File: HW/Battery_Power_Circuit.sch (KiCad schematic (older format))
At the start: 10 parts

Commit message: What did I do?
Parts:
- removed BT? (x2): Battery, symbol Battery
- added BT? (x2): 18650, symbol Battery_Cell
- added D?: 1N4448W, symbol D_ALT
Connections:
- wire segments 29 -> 33
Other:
- note added: "+"
- note added: "-"
- note added: "3.7V"
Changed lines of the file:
@@
 $EndDescr
-$Comp
-L Battery BT?
-U 1 1 5B317E9C
-P 6800 2400
-F 0 "BT?" H 6900 2500 50  0000 L CNN
-F 1 "Battery" H 6900 2400 50  0000 L CNN
-F 2 "" V 6800 2460 50  0001 C CNN
-F 3 "" V 6800 2460 50  0001 C CNN
-	1    6800 2400
-	1    0    0    -1
-$EndComp
-$Comp
-L Battery BT?
-U 1 1 5B32E42C
-P 6500 3750
-F 0 "BT?" H 6150 3850 50  0000 L CNN
-F 1 "Battery" H 6150 3750 50  0000 L CNN
-F 2 "" V 6500 3810 50  0001 C CNN
-F 3 "" V 6500 3810 50  0001 C CNN
-	1    6500 3750
-	1    0    0    -1
-$EndComp
 $Comp
 L VBUS #PWR?
@@
 NoConn ~ 6300 3350
 Wire Wire Line
-	6500 3350 6500 3550
+	6500 3350 6500 3600
 Wire Wire Line
 	6800 2750 6800 2600
 Wire Wire Line
-	6800 1850 6800 2200
+	6800 1850 6800 2300
 Wire Wire Line
 	6050 2000 6800 2000
@@
 	6900 4050 6500 4050
 Wire Wire Line
-	6500 3950 6500 4150
+	6500 3900 6500 4150
 $Comp
 L GND #PWR?
@@
 Wire Notes Line
 	3300 4650 5950 4650
+$Comp
+L Battery_Cell BT?
+U 1 1 5B34706B
+P 6500 3800
+F 0 "BT?" H 6600 3950 50  0000 L CNN
+F 1 "18650" H 6500 3750 50  0000 L CNN
+F 2 "" V 6500 3860 50  0001 C CNN
+F 3 "" V 6500 3860 50  0001 C CNN
+	1    6500 3800
+	1    0    0    -1
+$EndComp
+$Comp
+L Battery_Cell BT?
+U 1 1 5B3470A3
+P 6800 2500
+F 0 "BT?" H 6900 2600 50  0000 L CNN
+F 1 "18650" H 6900 2500 50  0000 L CNN
+F 2 "" V 6800 2560 50  0001 C CNN
+F 3 "" V 6800 2560 50  0001 C CNN
+	1    6800 2500
+	1    0    0    -1
+$EndComp
+Text Notes 6500 2500 0    60   ~ 0
+3.7V
+Text Notes 6150 3800 0    60   ~ 0
+3.7V
+Text Notes 6300 3700 0    60   ~ 0
++
+Text Notes 6300 3900 0    60   ~ 0
+-
+Text Notes 6650 2400 0    60   ~ 0
++
+Text Notes 6650 2600 0    60   ~ 0
+-
+$Comp
+L D_ALT D?
+U 1 1 5B34A2E5
+P 7700 3050
+F 0 "D?" H 7700 3150 50  0000 C CNN
+F 1 "1N4448W" H 7700 2950 50  0000 C CNN
+F 2 "" H 7700 3050 50  0001 C CNN
+F 3 "" H 7700 3050 50  0001 C CNN
+	1    7700 3050
+	0    1    1    0
+$EndComp
+Wire Wire Line
+	7700 2900 7700 2600
+Wire Wire Line
+	7700 2600 7200 2600
+Connection ~ 7200 2600
+Wire Wire Line
+	7700 3200 7700 3450
+Wire Wire Line
+	7700 3450 7200 3450
+Connection ~ 7200 3450
 $EndSCHEMATC

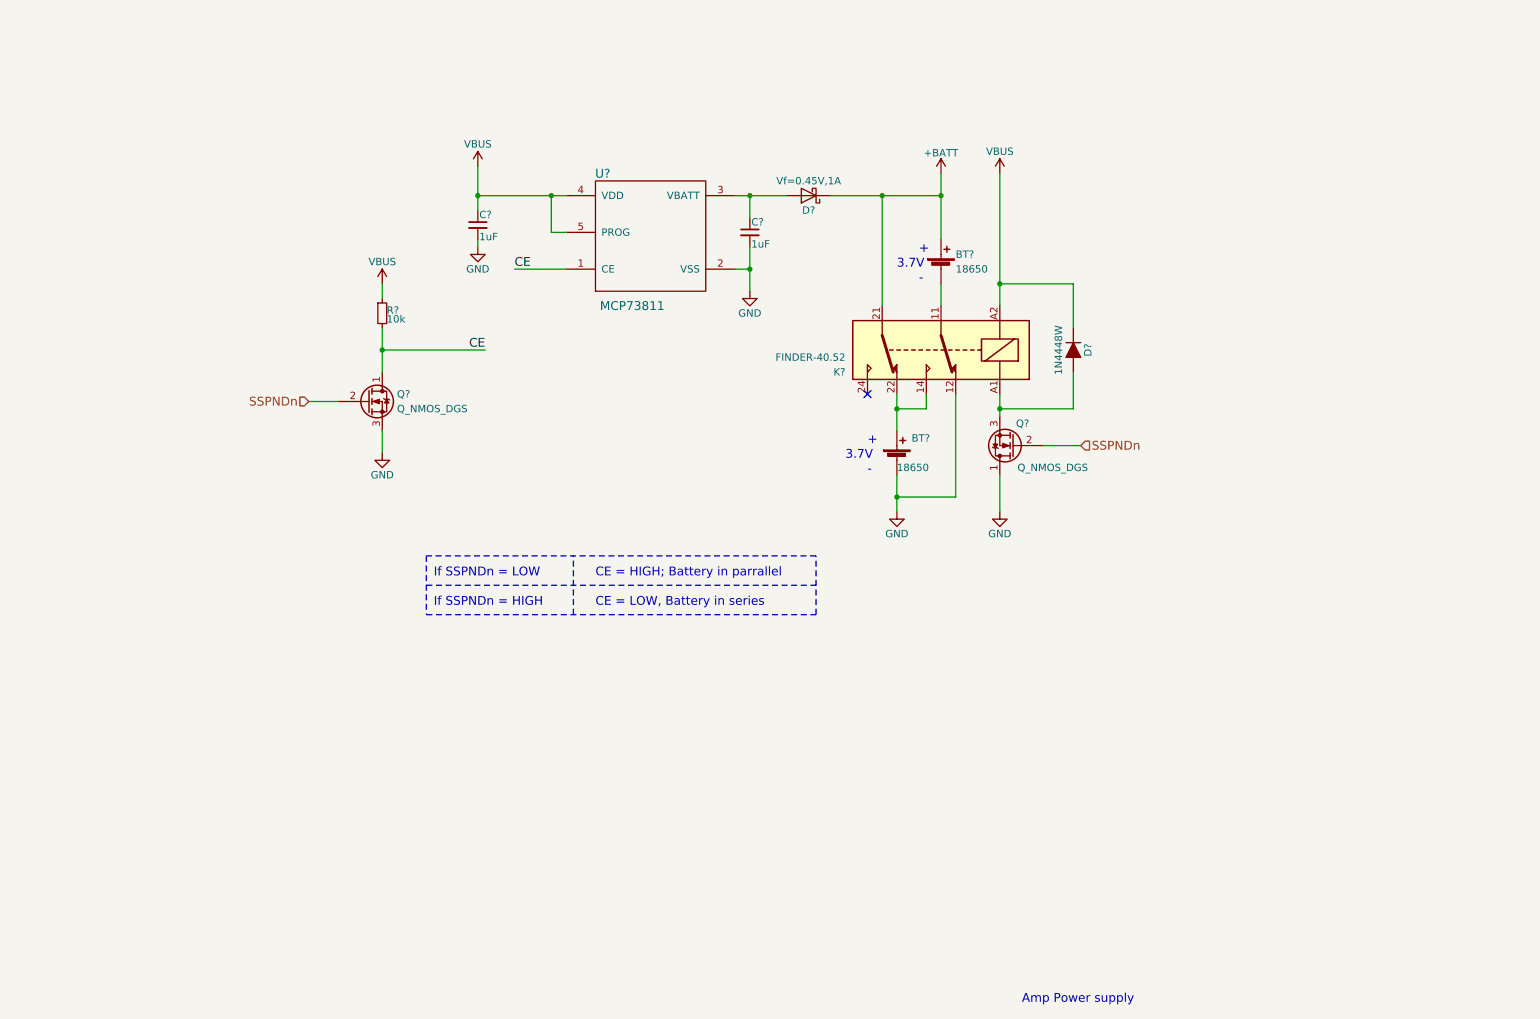
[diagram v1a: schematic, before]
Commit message: Added LEDs, Test points, and ESD protection on USB
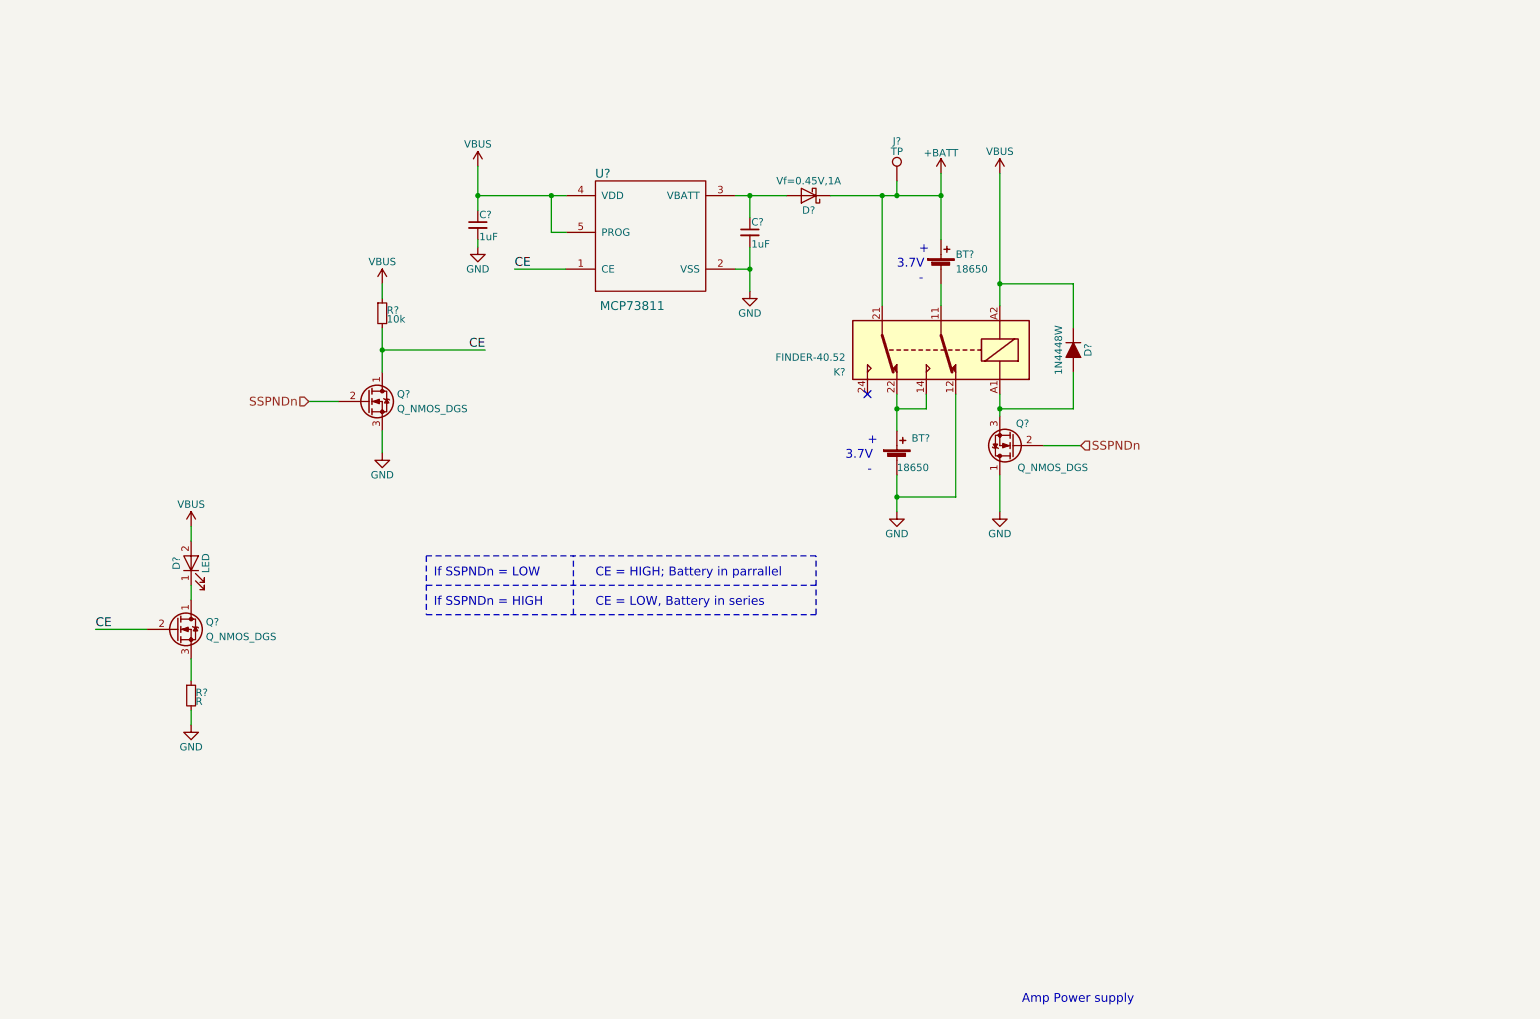
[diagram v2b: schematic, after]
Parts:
- added D?: LED, symbol LED
- added J?: TP, symbol TEST_1P
- added Q?: Q_NMOS_DGS, symbol Q_NMOS_DGS
- added R?: R, symbol R_Small
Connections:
- net +BATT: now also J?.1
- net CE: now also Q?.2 (G)
- net GND: now also R?.2
- net VBUS: now also D?.2 (A)
- new net: D?.1 (K), Q?.1 (D)
- new net: Q?.3 (S), R?.1
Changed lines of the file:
@@
 $EndComp
 Wire Wire Line
-	7200 2750 7200 1850
+	7200 1850 7200 2750
 $Comp
 L Q_NMOS_DGS Q?
@@
 $EndComp
 Wire Wire Line
-	7200 3500 7200 3350
+	7200 3350 7200 3500
 $Comp
 L GND #PWR?
@@
 	7700 3450 7200 3450
 Connection ~ 7200 3450
+$Comp
+L VBUS #PWR?
+U 1 1 5B3D1057
+P 1700 4250
+F 0 "#PWR?" H 1700 4100 50  0001 C CNN
+F 1 "VBUS" H 1700 4400 50  0000 C CNN
+F 2 "" H 1700 4250 50  0001 C CNN
+F 3 "" H 1700 4250 50  0001 C CNN
+	1    1700 4250
+	1    0    0    -1
+$EndComp
+$Comp
+L Q_NMOS_DGS Q?
+U 1 1 5B3D117C
+P 1600 4950
+F 0 "Q?" H 1800 5000 50  0000 L CNN
+F 1 "Q_NMOS_DGS" H 1800 4900 50  0000 L CNN
+F 2 "" H 1800 5050 50  0001 C CNN
+F 3 "" H 1600 4950 50  0001 C CNN
+	1    1600 4950
+	1    0    0    -1
+$EndComp
+$Comp
+L LED D?
+U 1 1 5B3D11DA
+P 1700 4500
+F 0 "D?" H 1700 4600 50  0000 C CNN
+F 1 "LED" H 1700 4400 50  0000 C CNN
+F 2 "" H 1700 4500 50  0001 C CNN
+F 3 "" H 1700 4500 50  0001 C CNN
+	1    1700 4500
+	0    -1   -1   0
+$EndComp
+Wire Wire Line
+	1700 4750 1700 4650
+Wire Wire Line
+	1700 4350 1700 4250
+Wire Wire Line
+	1400 4950 1050 4950
+Text Label 1050 4950 0    60   ~ 0
+CE
+$Comp
+L R_Small R?
+U 1 1 5B3D1363
+P 1700 5400
+F 0 "R?" H 1730 5420 50  0000 L CNN
+F 1 "R" H 1730 5360 50  0000 L CNN
+F 2 "" H 1700 5400 50  0001 C CNN
+F 3 "" H 1700 5400 50  0001 C CNN
+	1    1700 5400
+	1    0    0    -1
+$EndComp
+Wire Wire Line
+	1700 5300 1700 5150
+$Comp
+L GND #PWR?
+U 1 1 5B3D141A
+P 1700 5600
+F 0 "#PWR?" H 1700 5350 50  0001 C CNN
+F 1 "GND" H 1700 5450 50  0000 C CNN
+F 2 "" H 1700 5600 50  0001 C CNN
+F 3 "" H 1700 5600 50  0001 C CNN
+	1    1700 5600
+	1    0    0    -1
+$EndComp
+Wire Wire Line
+	1700 5600 1700 5500
+$Comp
+L TEST_1P J?
+U 1 1 5B3D6BCB
+P 6500 1900
+F 0 "J?" H 6500 2170 50  0000 C CNN
+F 1 "TP" H 6500 2100 50  0000 C CNN
+F 2 "" H 6700 1900 50  0001 C CNN
+F 3 "" H 6700 1900 50  0001 C CNN
+	1    6500 1900
+	1    0    0    -1
+$EndComp
+Wire Wire Line
+	6500 1900 6500 2000
+Connection ~ 6500 2000
 $EndSCHEMATC

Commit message: First draft done :100:
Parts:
- added C?: 1uF, symbol C_Small
- added C?: 10uF, symbol CP1_Small
- added D?: 1N4448W, symbol D_ALT
- added Q?: Q_NMOS_DGS, symbol Q_NMOS_DGS
- added U?: BA07CC0FP-E2, TO_SOT_Packages_THT:TO-252-2, symbol LF25_TO252
- D7: renamed from D?; value LED -> LED, 2.1V, 20mA
- R25: renamed from R?; value R -> 100
- gave numbers to parts that had none: 13
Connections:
- wire segments 39 -> 53
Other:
- note added: "Battery Charger"
- note added: "Battery Regulator"
- note added: "CE = LOW; Battery in series"
- note removed: "CE = LOW, Battery in series"
- moved on the sheet: J14

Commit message: First draft done :100:
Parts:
- gave numbers to parts that had none: 5

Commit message: 7V Regulator now a 5V buck converter
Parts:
- removed C75: 1uF, symbol C_Small
- removed C76: 10uF, symbol CP1_Small
- removed D15: 1N4448W, symbol D_ALT
- removed J7: TP, symbol TEST_1P
- removed Q9: Q_NMOS_DGS, symbol Q_NMOS_DGS
- removed U10: BA07CC0FP-E2, TO_SOT_Packages_THT:TO-252-2, symbol LF25_TO252
- added C?: 100uF, symbol CP1_Small
- added C?: 330uF, symbol CP1_Small
- added C?: NP, symbol CP1_Small
- added D?: 1N5819, symbol D_Schottky
- added L?: 330uH, symbol L
- added L?: 20uH, symbol L
- added R?: 0.0, symbol R
- added U?: TL2575, symbol TL2575
- D5: value Vf=0.45V,1A -> 1N5819
- K1: value FINDER-40.52 -> V23105A5001A201
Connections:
- net labels added: +5V
- wire segments 53 -> 61
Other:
- note added: "Buck Converter \n5V fixed output\n"
- note removed: "Battery Regulator"
- moved on the sheet: BT1, BT2, C35, C36, D5, D6, D7, K1, Q2, Q3, Q4, R24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

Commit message: Buck and fp
Changed buck to one with 3A output. Started fp association
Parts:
- removed U?: TL2575, symbol TL2575
- added U5: LM2576, TO_SOT_Packages_SMD:TO-263-5_TabPin6, symbol LM2576
- L8: renamed from L?; value 20uH -> NP
- R16: renamed from R?; footprint (none) -> Resistors_SMD:R_0805_HandSoldering
- R24, R25: footprint (none) -> Resistors_SMD:R_0805_HandSoldering
- gave numbers to parts that had none: 5
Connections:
- net +BATT: now also U5.1 (Vin)
- net GND: now also U5.3 (GND), U5.6 (GND)
- net SSPNDn: now also U5.5 (ENABLEn)
- net at D3.1 (K), L9.1: now also U5.2 (Vout), U5.4 (FEEDBACK)
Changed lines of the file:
@@
 $EndDescr
 $Comp
-L VBUS #PWR46
+L VBUS #PWR044
 U 1 1 5B32E869
 P 3100 1250
-AR Path="/5B42C84F/5B32E869" Ref="#PWR46"  Part="1"
+AR Path="/5B42C84F/5B32E869" Ref="#PWR044"  Part="1"
 AR Path="/5B429541/5B317E48/5B32E869" Ref="#PWR103"  Part="1"
-F 0 "#PWR46" H 3100 1100 50  0001 C CNN
+F 0 "#PWR044" H 3100 1100 50  0001 C CNN
 F 1 "VBUS" H 3100 1400 50  0000 C CNN
 F 2 "" H 3100 1250 50  0001 C CNN
@@
 NoConn ~ 5750 2800
 $Comp
-L GND #PWR56
+L GND #PWR045
 U 1 1 5B32F182
 P 5950 3600
-AR Path="/5B42C84F/5B32F182" Ref="#PWR56"  Part="1"
+AR Path="/5B42C84F/5B32F182" Ref="#PWR045"  Part="1"
 AR Path="/5B429541/5B317E48/5B32F182" Ref="#PWR113"  Part="1"
-F 0 "#PWR56" H 5950 3350 50  0001 C CNN
+F 0 "#PWR045" H 5950 3350 50  0001 C CNN
 F 1 "GND" H 5950 3450 50  0000 C CNN
 F 2 "" H 5950 3600 50  0001 C CNN
@@
 $EndComp
 $Comp
-L GND #PWR54
+L GND #PWR046
 U 1 1 5B32FAF2
 P 4950 2100
-AR Path="/5B42C84F/5B32FAF2" Ref="#PWR54"  Part="1"
+AR Path="/5B42C84F/5B32FAF2" Ref="#PWR046"  Part="1"
 AR Path="/5B429541/5B317E48/5B32FAF2" Ref="#PWR111"  Part="1"
-F 0 "#PWR54" H 4950 1850 50  0001 C CNN
+F 0 "#PWR046" H 4950 1850 50  0001 C CNN
 F 1 "GND" H 4950 1950 50  0000 C CNN
 F 2 "" H 4950 2100 50  0001 C CNN
@@
 $EndComp
 $Comp
-L GND #PWR49
+L GND #PWR047
 U 1 1 5B32FEF0
 P 3100 1800
-AR Path="/5B42C84F/5B32FEF0" Ref="#PWR49"  Part="1"
+AR Path="/5B42C84F/5B32FEF0" Ref="#PWR047"  Part="1"
 AR Path="/5B429541/5B317E48/5B32FEF0" Ref="#PWR106"  Part="1"
-F 0 "#PWR49" H 3100 1550 50  0001 C CNN
+F 0 "#PWR047" H 3100 1550 50  0001 C CNN
 F 1 "GND" H 3100 1650 50  0000 C CNN
 F 2 "" H 3100 1800 50  0001 C CNN
@@
 $EndComp
 $Comp
-L VBUS #PWR53
+L VBUS #PWR048
 U 1 1 5B330C0A
 P 1450 950
-AR Path="/5B42C84F/5B330C0A" Ref="#PWR53"  Part="1"
+AR Path="/5B42C84F/5B330C0A" Ref="#PWR048"  Part="1"
 AR Path="/5B429541/5B317E48/5B330C0A" Ref="#PWR110"  Part="1"
-F 0 "#PWR53" H 1450 800 50  0001 C CNN
+F 0 "#PWR048" H 1450 800 50  0001 C CNN
 F 1 "VBUS" H 1450 1100 50  0000 C CNN
 F 2 "" H 1450 950 50  0001 C CNN
@@
 $EndComp
 $Comp
-L GND #PWR55
+L GND #PWR049
 U 1 1 5B330CC3
 P 1450 2100
-AR Path="/5B42C84F/5B330CC3" Ref="#PWR55"  Part="1"
+AR Path="/5B42C84F/5B330CC3" Ref="#PWR049"  Part="1"
 AR Path="/5B429541/5B317E48/5B330CC3" Ref="#PWR112"  Part="1"
-F 0 "#PWR55" H 1450 1850 50  0001 C CNN
+F 0 "#PWR049" H 1450 1850 50  0001 C CNN
 F 1 "GND" H 1450 1950 50  0000 C CNN
 F 2 "" H 1450 2100 50  0001 C CNN
@@
 F 0 "R24" H 1480 1170 50  0000 L CNN
 F 1 "10k" H 1480 1110 50  0000 L CNN
-F 2 "" H 1450 1150 50  0001 C CNN
+F 2 "Resistors_SMD:R_0805_HandSoldering" H 1450 1150 50  0001 C CNN
 F 3 "" H 1450 1150 50  0001 C CNN
 	1    1450 1150
@@
 Amp Power supply
 $Comp
-L VBUS #PWR48
+L VBUS #PWR050
 U 1 1 5B336A6E
 P 6650 1700
-AR Path="/5B42C84F/5B336A6E" Ref="#PWR48"  Part="1"
+AR Path="/5B42C84F/5B336A6E" Ref="#PWR050"  Part="1"
 AR Path="/5B429541/5B317E48/5B336A6E" Ref="#PWR105"  Part="1"
-F 0 "#PWR48" H 6650 1550 50  0001 C CNN
+F 0 "#PWR050" H 6650 1550 50  0001 C CNN
 F 1 "VBUS" H 6650 1850 50  0000 C CNN
 F 2 "" H 6650 1700 50  0001 C CNN
@@
 $EndComp
 $Comp
-L GND #PWR57
+L GND #PWR051
 U 1 1 5B336F59
 P 6650 3600
-AR Path="/5B42C84F/5B336F59" Ref="#PWR57"  Part="1"
+AR Path="/5B42C84F/5B336F59" Ref="#PWR051"  Part="1"
 AR Path="/5B429541/5B317E48/5B336F59" Ref="#PWR114"  Part="1"
-F 0 "#PWR57" H 6650 3350 50  0001 C CNN
+F 0 "#PWR051" H 6650 3350 50  0001 C CNN
 F 1 "GND" H 6650 3450 50  0000 C CNN
 F 2 "" H 6650 3600 50  0001 C CNN
@@
 F 0 "R25" H 2730 3620 50  0000 L CNN
 F 1 "100" H 2750 3550 50  0000 L CNN
-F 2 "" H 2700 3600 50  0001 C CNN
+F 2 "Resistors_SMD:R_0805_HandSoldering" H 2700 3600 50  0001 C CNN
 F 3 "" H 2700 3600 50  0001 C CNN
 	1    2700 3600
@@
 $EndComp
 $Comp
-L GND #PWR59
+L GND #PWR052
 U 1 1 5B3D141A
 P 2700 3800
-AR Path="/5B42C84F/5B3D141A" Ref="#PWR59"  Part="1"
+AR Path="/5B42C84F/5B3D141A" Ref="#PWR052"  Part="1"
 AR Path="/5B429541/5B317E48/5B3D141A" Ref="#PWR116"  Part="1"
-F 0 "#PWR59" H 2700 3550 50  0001 C CNN
+F 0 "#PWR052" H 2700 3550 50  0001 C CNN
 F 1 "GND" H 2700 3650 50  0000 C CNN
 F 2 "" H 2700 3800 50  0001 C CNN
@@
 P 2700 2450
 AR Path="/5B429541/5B317E48/5B42F4A3" Ref="#PWR115"  Part="1"
-AR Path="/5B42C84F/5B42F4A3" Ref="#PWR58"  Part="1"
-F 0 "#PWR58" H 2700 2300 50  0001 C CNN
+AR Path="/5B42C84F/5B42F4A3" Ref="#PWR053"  Part="1"
+F 0 "#PWR053" H 2700 2300 50  0001 C CNN
 F 1 "+BATT" H 2700 2590 50  0000 C CNN
 F 2 "" H 2700 2450 50  0001 C CNN
@@
 Battery Charger
 $Comp
-L +BATT #PWR?
+L +BATT #PWR054
 U 1 1 5B442B24
 P 6250 1350
-F 0 "#PWR?" H 6250 1200 50  0001 C CNN
+F 0 "#PWR054" H 6250 1200 50  0001 C CNN
 F 1 "+BATT" H 6250 1490 50  0000 C CNN
 F 2 "" H 6250 1350 50  0001 C CNN
@@
 $EndComp
 $Comp
-L +5V #PWR?
+L +5V #PWR055
 U 1 1 5B4435AD
 P 7100 4500
-F 0 "#PWR?" H 7100 4350 50  0001 C CNN
+F 0 "#PWR055" H 7100 4350 50  0001 C CNN
 F 1 "+5V" H 7100 4640 50  0000 C CNN
 F 2 "" H 7100 4500 50  0001 C CNN
@@
 $EndComp
 $Comp
-L TL2575 U?
-U 1 1 5B4445F3
-P 9250 5350
-F 0 "U?" H 9300 6450 60  0000 C CNN
-F 1 "TL2575" H 9400 5400 60  0000 C CNN
-F 2 "" H 9250 4400 60  0001 C CNN
-F 3 "" H 9250 4400 60  0001 C CNN
-	1    9250 5350
-	1    0    0    -1
-$EndComp
-$Comp
-L GND #PWR?
+L GND #PWR056
 U 1 1 5B444971
 P 8950 5500
-F 0 "#PWR?" H 8950 5250 50  0001 C CNN
+F 0 "#PWR056" H 8950 5250 50  0001 C CNN
 F 1 "GND" H 8950 5350 50  0000 C CNN
 F 2 "" H 8950 5500 50  0001 C CNN
@@
 $EndComp
 $Comp
-L GND #PWR?
+L GND #PWR057
 U 1 1 5B4449D0
 P 10700 5250
-F 0 "#PWR?" H 10700 5000 50  0001 C CNN
+F 0 "#PWR057" H 10700 5000 50  0001 C CNN
 F 1 "GND" H 10700 5100 50  0000 C CNN
 F 2 "" H 10700 5250 50  0001 C CNN
@@
 SSPNDn
 $Comp
-L CP1_Small C?
+L CP1_Small C37
 U 1 1 5B446257
 P 8500 4050
-F 0 "C?" H 8510 4120 50  0000 L CNN
+F 0 "C37" H 8510 4120 50  0000 L CNN
 F 1 "100uF" H 8510 3970 50  0000 L CNN
 F 2 "" H 8500 4050 50  0001 C CNN
@@
 $EndComp
 $Comp
-L +BATT #PWR?
+L +BATT #PWR058
 U 1 1 5B447866
 P 8500 3750
-F 0 "#PWR?" H 8500 3600 50  0001 C CNN
+F 0 "#PWR058" H 8500 3600 50  0001 C CNN
 F 1 "+BATT" H 8500 3890 50  0000 C CNN
 F 2 "" H 8500 3750 50  0001 C CNN
@@
 $EndComp
 $Comp
-L GND #PWR?
+L GND #PWR059
 U 1 1 5B4478B3
 P 8500 4250
-F 0 "#PWR?" H 8500 4000 50  0001 C CNN
+F 0 "#PWR059" H 8500 4000 50  0001 C CNN
 F 1 "GND" H 8500 4100 50  0000 C CNN
 F 2 "" H 8500 4250 50  0001 C CNN
@@
 $EndComp
 $Comp
-L CP1_Small C?
+L CP1_Small C39
 U 1 1 5B4496FA
 P 7850 5350
-F 0 "C?" H 7860 5420 50  0000 L CNN
+F 0 "C39" H 7860 5420 50  0000 L CNN
 F 1 "330uF" H 7860 5270 50  0000 L CNN
 F 2 "" H 7850 5350 50  0001 C CNN
@@
 $EndComp
 $Comp
-L GND #PWR?
+L GND #PWR060
 U 1 1 5B4497AF
 P 7850 5550
-F 0 "#PWR?" H 7850 5300 50  0001 C CNN
+F 0 "#PWR060" H 7850 5300 50  0001 C CNN
 F 1 "GND" H 7850 5400 50  0000 C CNN
 F 2 "" H 7850 5550 50  0001 C CNN
@@
 $EndComp
 $Comp
-L D_Schottky D?
+L D_Schottky D3
 U 1 1 5B44A163
 P 8500 5200
-F 0 "D?" V 8400 5300 50  0000 C CNN
+F 0 "D3" V 8400 5300 50  0000 C CNN
 F 1 "1N5819" V 8500 5400 50  0000 C CNN
 F 2 "" H 8500 5200 50  0001 C CNN
@@
 	8500 4750 8500 5050
 $Comp
-L GND #PWR?
+L GND #PWR061
 U 1 1 5B44B4E2
 P 8500 5450
-F 0 "#PWR?" H 8500 5200 50  0001 C CNN
+F 0 "#PWR061" H 8500 5200 50  0001 C CNN
 F 1 "GND" H 8500 5300 50  0000 C CNN
 F 2 "" H 8500 5450 50  0001 C CNN
@@
 	8300 4750 9050 4750
 $Comp
-L L L?
+L L L9
 U 1 1 5B44C1D8
 P 8150 4750
-F 0 "L?" V 8100 4750 50  0000 C CNN
+F 0 "L9" V 8100 4750 50  0000 C CNN
 F 1 "330uH" V 8225 4750 50  0000 C CNN
 F 2 "" H 8150 4750 50  0001 C CNN
@@
 Connection ~ 8500 3850
 $Comp
-L L L?
+L L L8
 U 1 1 5B451413
 P 7450 4750
-F 0 "L?" V 7400 4750 50  0000 C CNN
-F 1 "20uH" V 7525 4750 50  0000 C CNN
+F 0 "L8" V 7400 4750 50  0000 C CNN
+F 1 "NP" V 7525 4750 50  0000 C CNN
 F 2 "" H 7450 4750 50  0001 C CNN
 F 3 "" H 7450 4750 50  0001 C CNN
@@
 $EndComp
 $Comp
-L CP1_Small C?
+L CP1_Small C38
 U 1 1 5B451492
 P 7100 5350
-F 0 "C?" H 7110 5420 50  0000 L CNN
+F 0 "C38" H 7110 5420 50  0000 L CNN
 F 1 "NP" H 7110 5270 50  0000 L CNN
 F 2 "" H 7100 5350 50  0001 C CNN
@@
 $EndComp
 $Comp
-L GND #PWR?
+L GND #PWR062
 U 1 1 5B451498
 P 7100 5550
-F 0 "#PWR?" H 7100 5300 50  0001 C CNN
+F 0 "#PWR062" H 7100 5300 50  0001 C CNN
 F 1 "GND" H 7100 5400 50  0000 C CNN
 F 2 "" H 7100 5550 50  0001 C CNN
@@
 Connection ~ 7100 4750
 $Comp
-L R R?
+L R R16
 U 1 1 5B4516BC
 P 7450 5000
-F 0 "R?" V 7530 5000 50  0000 C CNN
+F 0 "R16" V 7530 5000 50  0000 C CNN
 F 1 "0.0" V 7450 5000 50  0000 C CNN
-F 2 "" V 7380 5000 50  0001 C CNN
+F 2 "Resistors_SMD:R_0805_HandSoldering" V 7380 5000 50  0001 C CNN
 F 3 "" H 7450 5000 50  0001 C CNN
 	1    7450 5000
@@
 Text Notes 9350 3850 0    60   ~ 0
 Buck Converter \n5V fixed output\n
+$Comp
+L LM2576 U5
+U 1 1 5B4544F5
+P 9250 5350
+F 0 "U5" H 9300 6450 60  0000 C CNN
+F 1 "LM2576" H 9450 5450 60  0000 C CNN
+F 2 "TO_SOT_Packages_SMD:TO-263-5_TabPin6" H 9250 4400 60  0001 C CNN
+F 3 "" H 9250 4400 60  0001 C CNN
+	1    9250 5350
+	1    0    0    -1
+$EndComp
 $EndSCHEMATC
